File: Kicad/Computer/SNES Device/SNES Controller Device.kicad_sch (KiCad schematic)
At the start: 0 parts

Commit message: Added a demo LSF0204 project.
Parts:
- added IC?: 74LVC1G08GV,125, SOT95P275X110-5N, symbol Nexperia:74LVC1G08GV,125
- added IC?: 74LVC2G32DP,125, SOP65P400X110-8N, symbol Nexperia:74LVC2G32DP,125
- added IC? (x2): 74ALVC32PW,118, SOP65P640X110-14N, symbol Nexperia:74ALVC32PW,118
- added IC?: 74LVC1G02GV,125, SOT95P275X110-5N, symbol Nexperia:74LVC1G02GV,125
- added IC?: 74LVC273PW,118, SOP65P640X110-20N, symbol Nexperia:74LVC273PW,118
- added IC? (x2): 74LVC541APW,118, SOP65P640X110-20N, symbol Nexperia:74LVC541APW,118
- added J?: HCP65_PCI_Express_x36_pin, Connector_PCBEdge:BUS_PCIexpress_x1, symbol HCP65:HCP65_PCI_Express_x36_pin
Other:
- added sheet Device Selector (Device Selector.kicad_sch)

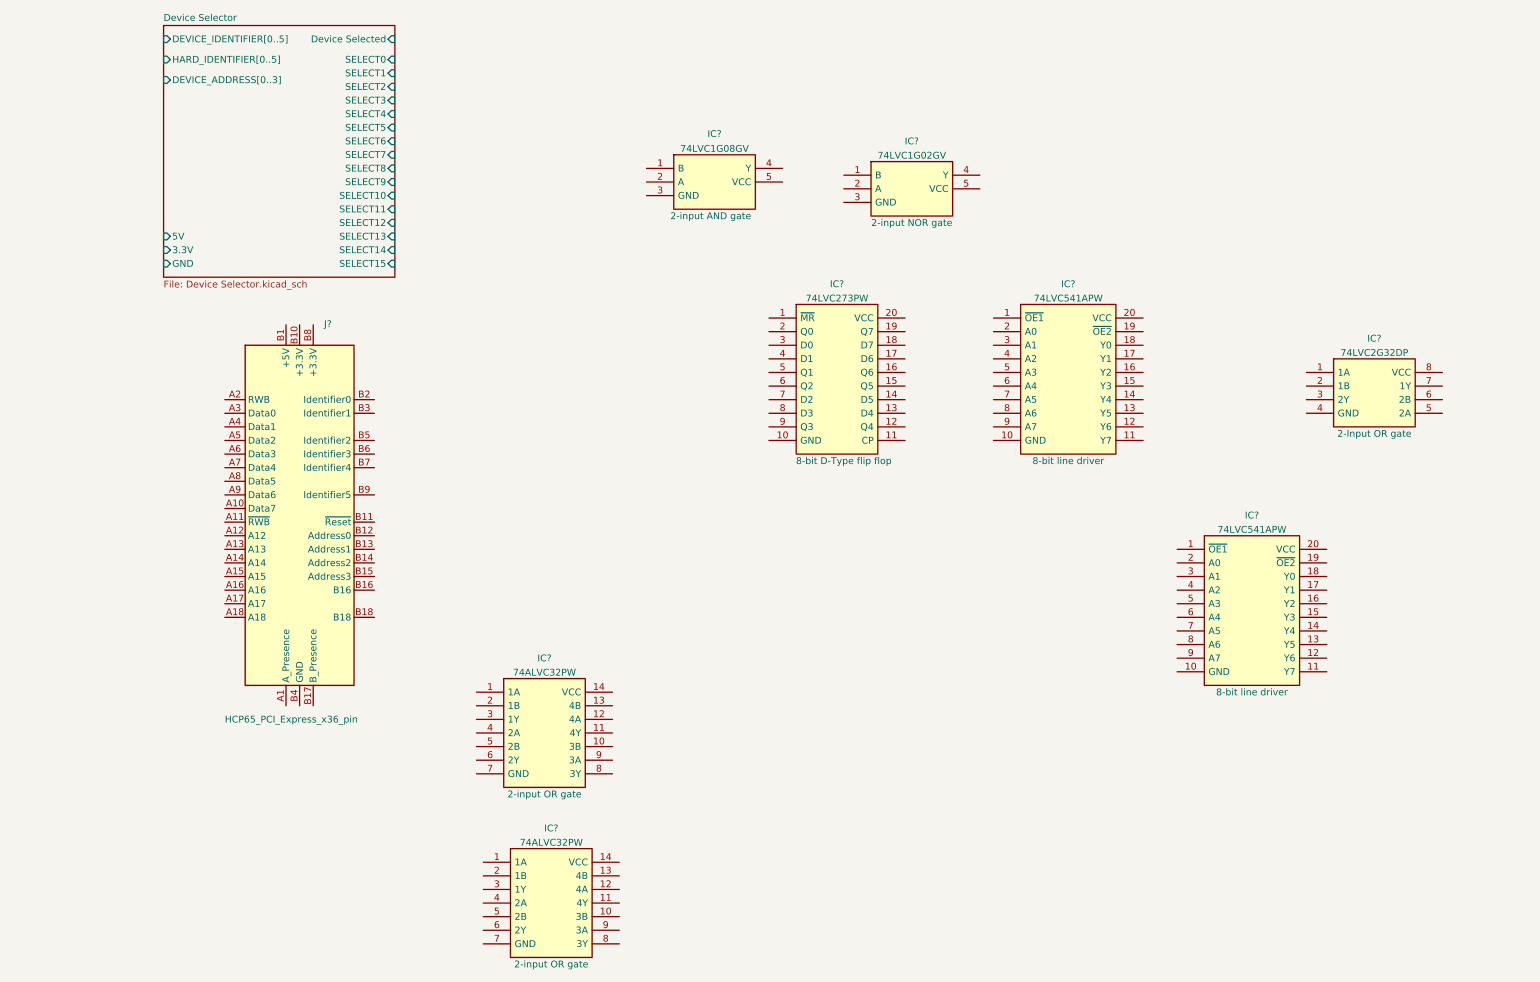
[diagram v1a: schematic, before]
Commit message: Splitting the SNES Device into even more boards.
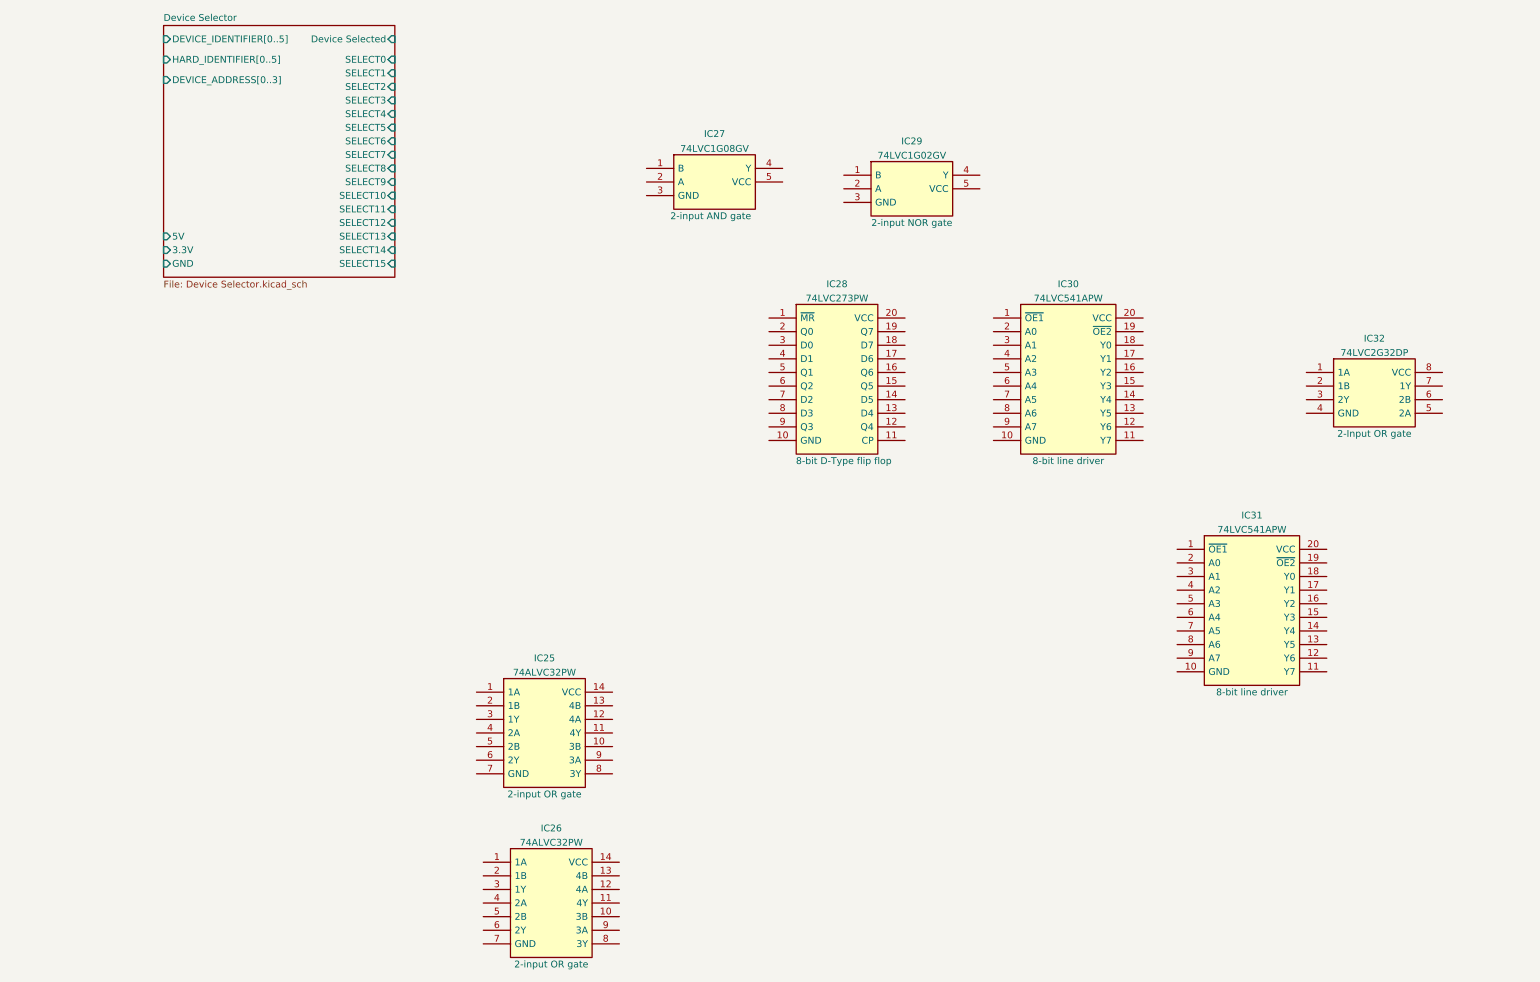
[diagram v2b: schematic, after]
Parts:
- removed J?: HCP65_PCI_Express_x36_pin, Connector_PCBEdge:BUS_PCIexpress_x1, symbol HCP65:HCP65_PCI_Express_x36_pin
- gave numbers to parts that had none: 8
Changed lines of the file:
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@@
   (symbol (lib_id "Nexperia:74LVC1G08GV,125") (at 129.54 44.45 0) (unit 1)
     (in_bom yes) (on_board yes) (fields_autoplaced)
-    (property "Reference" "IC?" (id 0) (at 142.24 37.9943 0))
+    (property "Reference" "IC27" (id 0) (at 142.24 37.9943 0))
     (property "Value" "74LVC1G08GV,125" (id 1) (at 151.13 39.37 0)
       (effects (font (size 1.27 1.27)) (justify left) hide)
@@
   (symbol (lib_id "Nexperia:74LVC2G32DP,125") (at 252.73 82.55 0) (unit 1)
     (in_bom yes) (on_board yes)
-    (property "Reference" "IC?" (id 0) (at 265.43 76.2 0))
+    (property "Reference" "IC32" (id 0) (at 265.43 76.2 0))
     (property "Value" "74LVC2G32DP,125" (id 1) (at 274.32 77.47 0)
       (effects (font (size 1.27 1.27)) (justify left) hide)
@@
   (symbol (lib_id "Nexperia:74ALVC32PW,118") (at 99.06 173.99 0) (unit 1)
     (in_bom yes) (on_board yes)
-    (property "Reference" "IC?" (id 0) (at 111.76 167.64 0))
+    (property "Reference" "IC26" (id 0) (at 111.76 167.64 0))
     (property "Value" "74ALVC32PW,118" (id 1) (at 120.65 168.91 0)
       (effects (font (size 1.27 1.27)) (justify left) hide)
@@
   (symbol (lib_id "Nexperia:74ALVC32PW,118") (at 97.79 142.24 0) (unit 1)
     (in_bom yes) (on_board yes)
-    (property "Reference" "IC?" (id 0) (at 110.49 135.89 0))
+    (property "Reference" "IC25" (id 0) (at 110.49 135.89 0))
     (property "Value" "74ALVC32PW,118" (id 1) (at 119.38 137.16 0)
       (effects (font (size 1.27 1.27)) (justify left) hide)
@@
     (pin "9")
   )
-  (symbol (lib_id "HCP65:HCP65_PCI_Express_x36_pin") (at 64.77 99.06 0) (unit 1)
-    (in_bom yes) (on_board yes)
-    (property "Reference" "J?" (id 0) (at 69.3294 73.5035 0)
-      (effects (font (size 1.27 1.27)) (justify left))
-    )
-    (property "Value" "HCP65_PCI_Express_x36_pin" (id 1) (at 50.8 147.32 0)
-      (effects (font (size 1.27 1.27)) (justify left))
-    )
-    (property "Footprint" "Connector_PCBEdge:BUS_PCIexpress_x1" (id 2) (at 64.77 60.96 0)
-      (effects (font (size 1.27 1.27)) hide)
-    )
-    (property "Datasheet" "" (id 3) (at 64.77 135.89 90)
-      (effects (font (size 1.27 1.27)) hide)
-    )
-    (pin "A1")
-    (pin "A10")
-    (pin "A11")
-    (pin "A12")
-    (pin "A13")
-    (pin "A14")
-    (pin "A15")
-    (pin "A16")
-    (pin "A17")
-    (pin "A18")
-    (pin "A2")
-    (pin "A3")
-    (pin "A4")
-    (pin "A5")
-    (pin "A6")
-    (pin "A7")
-    (pin "A8")
-    (pin "A9")
-    (pin "B1")
-    (pin "B10")
-    (pin "B11")
-    (pin "B12")
-    (pin "B13")
-    (pin "B14")
-    (pin "B15")
-    (pin "B16")
-    (pin "B17")
-    (pin "B18")
-    (pin "B2")
-    (pin "B3")
-    (pin "B4")
-    (pin "B5")
-    (pin "B6")
-    (pin "B7")
-    (pin "B8")
-    (pin "B9")
-  )
   (symbol (lib_id "Nexperia:74LVC1G02GV,125") (at 166.37 45.72 0) (unit 1)
     (in_bom yes) (on_board yes)
-    (property "Reference" "IC?" (id 0) (at 179.07 39.37 0))
+    (property "Reference" "IC29" (id 0) (at 179.07 39.37 0))
     (property "Value" "74LVC1G02GV,125" (id 1) (at 187.96 40.64 0)
       (effects (font (size 1.27 1.27)) (justify left) hide)
@@
   (symbol (lib_id "Nexperia:74LVC273PW,118") (at 152.4 72.39 0) (unit 1)
     (in_bom yes) (on_board yes)
-    (property "Reference" "IC?" (id 0) (at 165.1 66.04 0))
+    (property "Reference" "IC28" (id 0) (at 165.1 66.04 0))
     (property "Value" "74LVC273PW,118" (id 1) (at 173.99 67.31 0)
       (effects (font (size 1.27 1.27)) (justify left) hide)
@@
   (symbol (lib_id "Nexperia:74LVC541APW,118") (at 228.6 115.57 0) (unit 1)
     (in_bom yes) (on_board yes)
-    (property "Reference" "IC?" (id 0) (at 242.57 109.22 0))
+    (property "Reference" "IC31" (id 0) (at 242.57 109.22 0))
     (property "Value" "74LVC541APW,118" (id 1) (at 252.73 110.49 0)
       (effects (font (size 1.27 1.27)) (justify left) hide)
@@
   (symbol (lib_id "Nexperia:74LVC541APW,118") (at 194.31 72.39 0) (unit 1)
     (in_bom yes) (on_board yes)
-    (property "Reference" "IC?" (id 0) (at 208.28 66.04 0))
+    (property "Reference" "IC30" (id 0) (at 208.28 66.04 0))
     (property "Value" "74LVC541APW,118" (id 1) (at 218.44 67.31 0)
       (effects (font (size 1.27 1.27)) (justify left) hide)

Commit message: Connected the SNES Device interface thing.
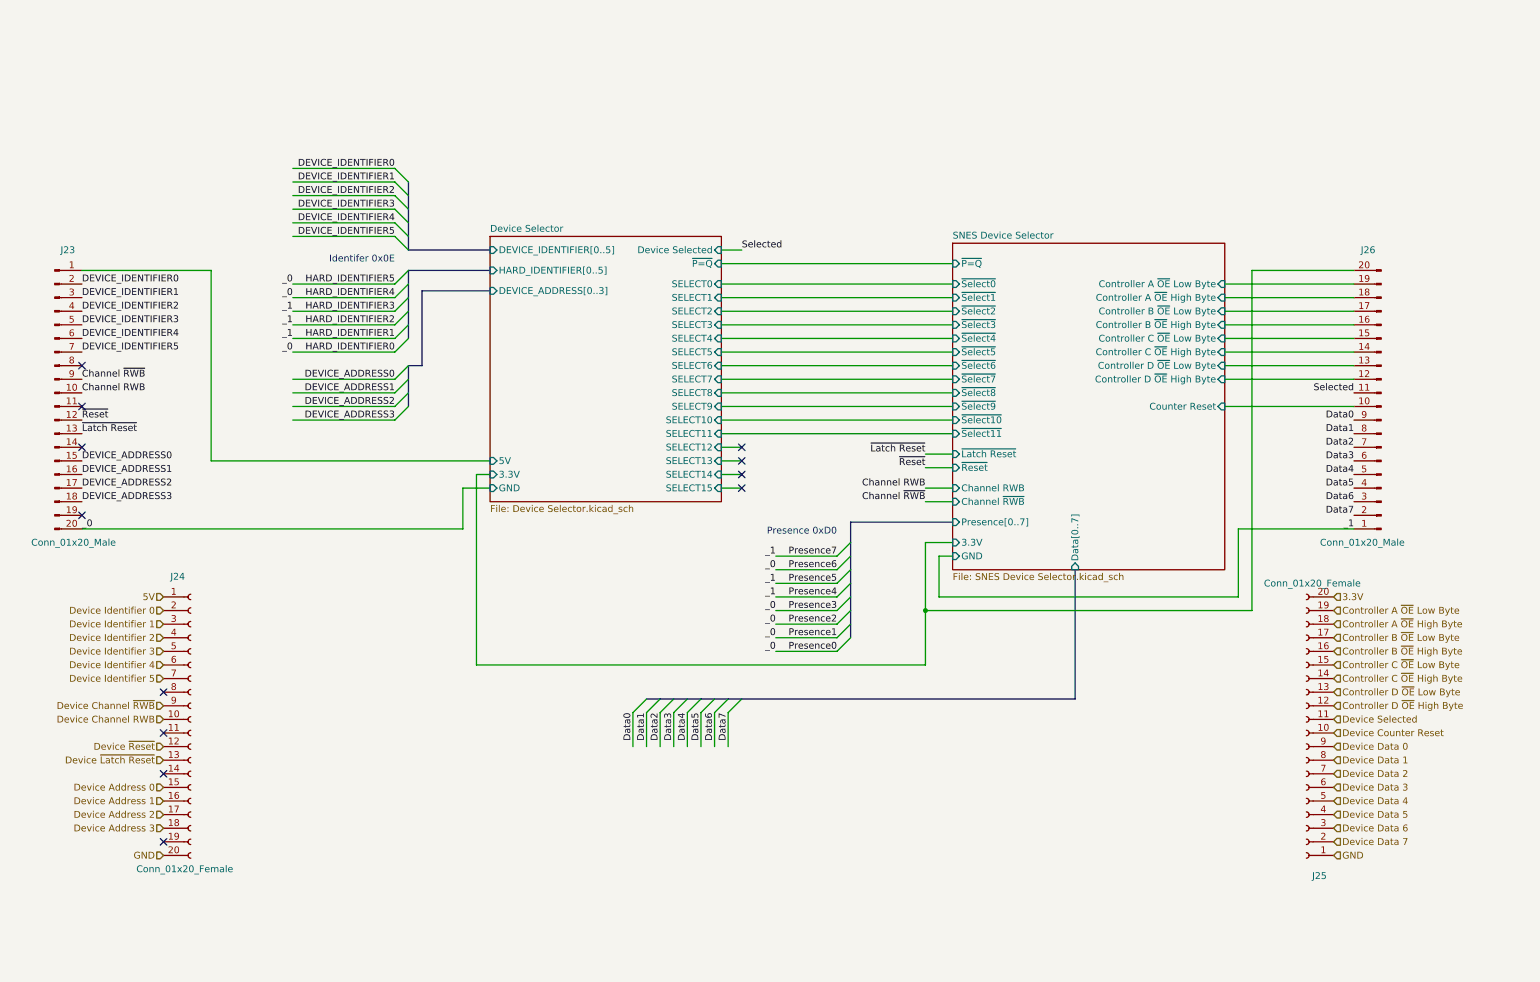
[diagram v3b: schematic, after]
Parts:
- removed IC25, IC26: 74ALVC32PW,118, SOP65P640X110-14N, symbol Nexperia:74ALVC32PW,118
- removed IC27: 74LVC1G08GV,125, SOT95P275X110-5N, symbol Nexperia:74LVC1G08GV,125
- removed IC28: 74LVC273PW,118, SOP65P640X110-20N, symbol Nexperia:74LVC273PW,118
- removed IC29: 74LVC1G02GV,125, SOT95P275X110-5N, symbol Nexperia:74LVC1G02GV,125
- removed IC30, IC31: 74LVC541APW,118, SOP65P640X110-20N, symbol Nexperia:74LVC541APW,118
- removed IC32: 74LVC2G32DP,125, SOP65P400X110-8N, symbol Nexperia:74LVC2G32DP,125
- added J23, J26: Conn_01x20_Male, Connector_PinHeader_2.54mm:PinHeader_1x20_P2.54mm_Vertical, symbol Connector:Conn_01x20_Male
- added J24, J25: Conn_01x20_Female, Connector_PinSocket_2.54mm:PinSocket_1x20_P2.54mm_Vertical, symbol Connector:Conn_01x20_Female
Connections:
- net Device Selector/3.3V: now also J26.20 (Pin_20)
- net Device Selector/5V: now also J23.1 (Pin_1)
- new net 3.3V: J25.20 (Pin_20)
- new net 5V: J24.1 (Pin_1)
- new net Channel RWB: J23.10 (Pin_10)
- new net Channel ~{RWB}: J23.9 (Pin_9)
- new net Controller A ~{OE} High Byte: J25.18 (Pin_18)
- new net Controller A ~{OE} Low Byte: J25.19 (Pin_19)
- new net Controller B ~{OE} High Byte: J25.16 (Pin_16)
- new net Controller B ~{OE} Low Byte: J25.17 (Pin_17)
- new net Controller C ~{OE} High Byte: J25.14 (Pin_14)
- new net Controller C ~{OE} Low Byte: J25.15 (Pin_15)
- new net Controller D ~{OE} High Byte: J25.12 (Pin_12)
- new net Controller D ~{OE} Low Byte: J25.13 (Pin_13)
- new net DEVICE_ADDRESS0: J23.15 (Pin_15)
- new net DEVICE_ADDRESS1: J23.16 (Pin_16)
- new net DEVICE_ADDRESS2: J23.17 (Pin_17)
- new net DEVICE_ADDRESS3: J23.18 (Pin_18)
- new net DEVICE_IDENTIFIER0: J23.2 (Pin_2)
- new net DEVICE_IDENTIFIER1: J23.3 (Pin_3)
- new net DEVICE_IDENTIFIER2: J23.4 (Pin_4)
- new net DEVICE_IDENTIFIER3: J23.5 (Pin_5)
- new net DEVICE_IDENTIFIER4: J23.6 (Pin_6)
- new net DEVICE_IDENTIFIER5: J23.7 (Pin_7)
- new net Data0: J26.9 (Pin_9)
- new net Data1: J26.8 (Pin_8)
- new net Data2: J26.7 (Pin_7)
- new net Data3: J26.6 (Pin_6)
- new net Data4: J26.5 (Pin_5)
- new net Data5: J26.4 (Pin_4)
- new net Data6: J26.3 (Pin_3)
- new net Data7: J26.2 (Pin_2)
- new net Device Address 0: J24.15 (Pin_15)
- new net Device Address 1: J24.16 (Pin_16)
- new net Device Address 2: J24.17 (Pin_17)
- new net Device Address 3: J24.18 (Pin_18)
- new net Device Channel RWB: J24.10 (Pin_10)
- new net Device Channel ~{RWB}: J24.9 (Pin_9)
- new net Device Counter Reset: J25.10 (Pin_10)
- new net Device Data 0: J25.9 (Pin_9)
- new net Device Data 1: J25.8 (Pin_8)
- new net Device Data 2: J25.7 (Pin_7)
- new net Device Data 3: J25.6 (Pin_6)
- new net Device Data 4: J25.5 (Pin_5)
- new net Device Data 5: J25.4 (Pin_4)
- new net Device Data 6: J25.3 (Pin_3)
- new net Device Data 7: J25.2 (Pin_2)
- new net Device Identifier 0: J24.2 (Pin_2)
- new net Device Identifier 1: J24.3 (Pin_3)
- new net Device Identifier 2: J24.4 (Pin_4)
- new net Device Identifier 3: J24.5 (Pin_5)
- new net Device Identifier 4: J24.6 (Pin_6)
- new net Device Identifier 5: J24.7 (Pin_7)
- new net Device Selected: J25.11 (Pin_11)
- new net Device ~{Latch Reset}: J24.13 (Pin_13)
- new net Device ~{Reset}: J24.12 (Pin_12)
- new net GND: J24.20 (Pin_20), J25.1 (Pin_1)
- new net HARD_IDENTIFIER0: J23.20 (Pin_20)
- new net HARD_IDENTIFIER1: J26.1 (Pin_1)
- new net SNES Device Selector/Controller A ~{OE} High Byte: J26.18 (Pin_18)
- new net SNES Device Selector/Controller A ~{OE} Low Byte: J26.19 (Pin_19)
- new net SNES Device Selector/Controller B ~{OE} High Byte: J26.16 (Pin_16)
- new net SNES Device Selector/Controller B ~{OE} Low Byte: J26.17 (Pin_17)
- new net SNES Device Selector/Controller C ~{OE} High Byte: J26.14 (Pin_14)
- new net SNES Device Selector/Controller C ~{OE} Low Byte: J26.15 (Pin_15)
- new net SNES Device Selector/Controller D ~{OE} High Byte: J26.12 (Pin_12)
- new net SNES Device Selector/Controller D ~{OE} Low Byte: J26.13 (Pin_13)
- new net SNES Device Selector/Counter Reset: J26.10 (Pin_10)
- new net Selected: J26.11 (Pin_11)
- new net ~{Latch Reset}: J23.13 (Pin_13)
- new net ~{Reset}: J23.12 (Pin_12)
- no-connect marks 0 -> 12
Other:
- added sheet SNES Device Selector (SNES Device Selector.kicad_sch)
- sheet Device Selector ports: added ~{P=Q}; removed none
- note added: "Identifer 0x0E"
- note added: "Presence 0xD0"
